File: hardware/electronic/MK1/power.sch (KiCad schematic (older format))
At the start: 3 parts

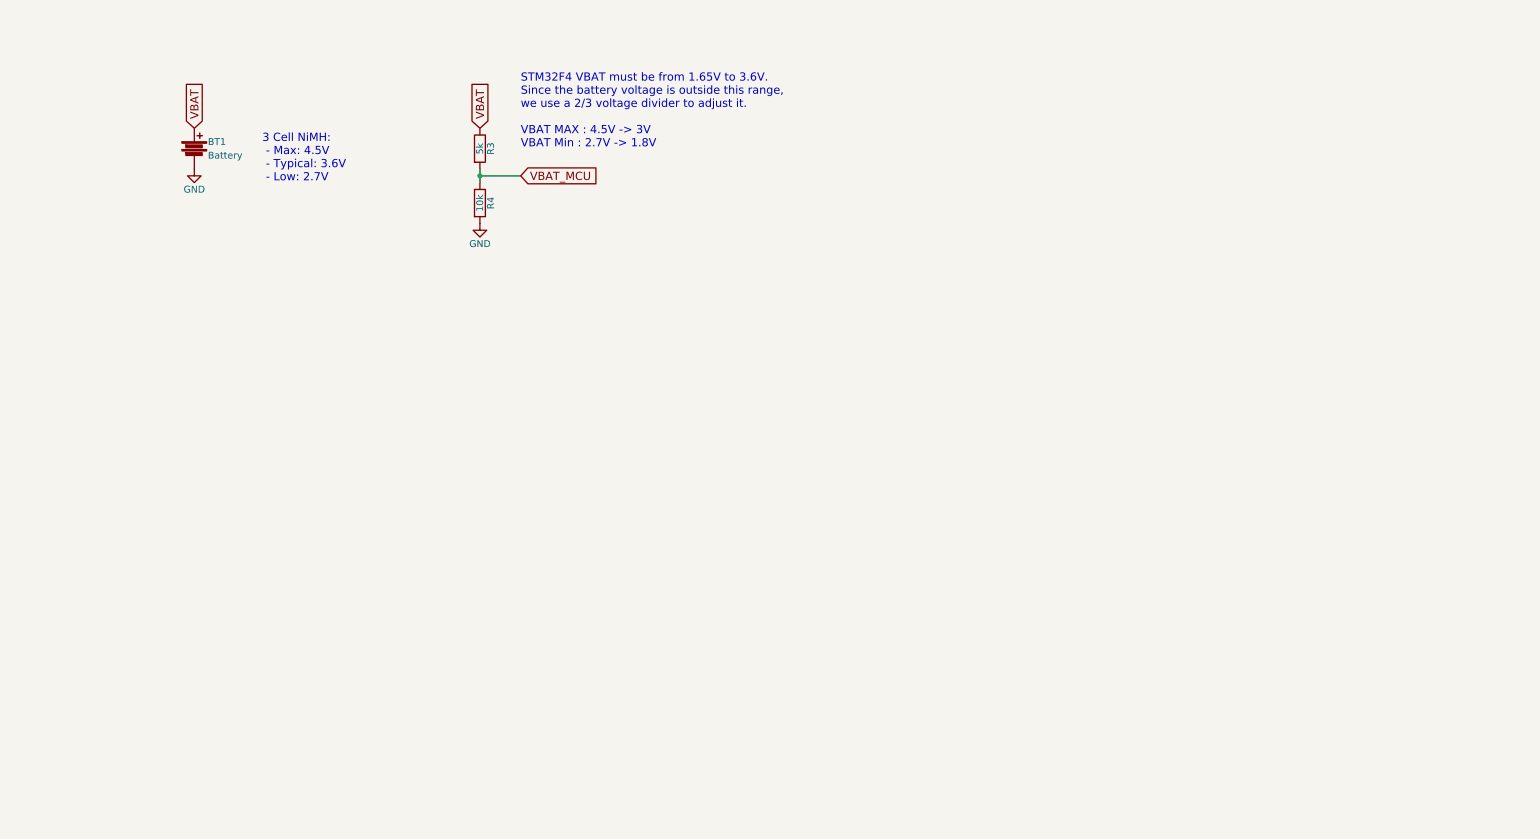
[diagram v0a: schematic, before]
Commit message: HW: Add 3V3 and 5V regulators
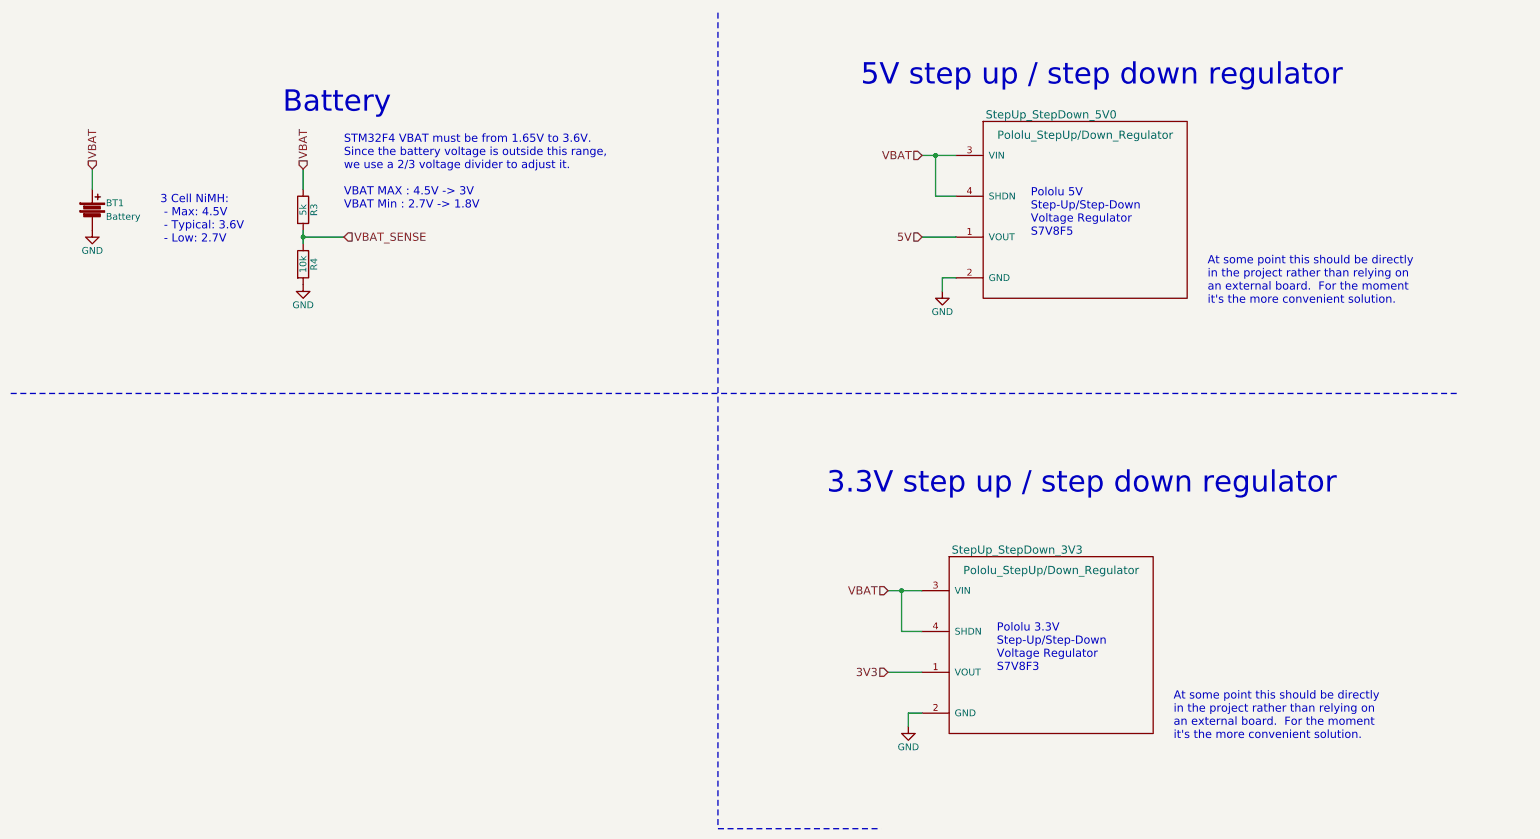
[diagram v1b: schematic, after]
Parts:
- added StepUp_StepDown_3V3, StepUp_StepDown_5V0: Pololu_StepUp/Down_Regulator, symbol Pololu_StepUp/Down_Regulator
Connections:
- net GND: now also StepUp_StepDown_3V3.2 (GND), StepUp_StepDown_5V0.2 (GND)
- net VBAT: now also StepUp_StepDown_3V3.3 (VIN), StepUp_StepDown_3V3.4 (SHDN), StepUp_StepDown_5V0.3 (VIN), StepUp_StepDown_5V0.4 (SHDN)
- net VBAT_MCU renamed VBAT_SENSE
- new net 3V3: StepUp_StepDown_3V3.1 (VOUT)
- new net 5V: StepUp_StepDown_5V0.1 (VOUT)
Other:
- note added: "3.3V step up / step down regulator"
- note added: "5V step up / step down regulator"
- note added: "At some point this should be directly \nin the project rather than relying on \nan external board. For the moment\nit's the more convenient solution."
- note added: "Battery"
- note added: "Pololu 3.3V \nStep-Up/Step-Down\nVoltage Regulator\nS7V8F3"
- note added: "Pololu 5V \nStep-Up/Step-Down\nVoltage Regulator\nS7V8F5"
- moved on the sheet: BT1, R3, R4
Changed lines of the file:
@@
 L Battery BT1
 U 1 1 5885FA38
-P 1900 1550
-F 0 "BT1" H 2000 1600 50  0000 L CNN
-F 1 "Battery" H 2000 1500 50  0000 L CNN
-F 2 "" V 1900 1590 50  0001 C CNN
-F 3 "" V 1900 1590 50  0000 C CNN
-	1    1900 1550
+P 1150 2000
+F 0 "BT1" H 1250 2050 50  0000 L CNN
+F 1 "Battery" H 1250 1950 50  0000 L CNN
+F 2 "" V 1150 2040 50  0001 C CNN
+F 3 "" V 1150 2040 50  0000 C CNN
+	1    1150 2000
 	1    0    0    -1
 $EndComp
@@
 L GND #PWR06
 U 1 1 5885FB0A
-P 1900 1700
-F 0 "#PWR06" H 1900 1450 50  0001 C CNN
-F 1 "GND" H 1900 1550 50  0000 C CNN
-F 2 "" H 1900 1700 50  0000 C CNN
-F 3 "" H 1900 1700 50  0000 C CNN
-	1    1900 1700
+P 1150 2150
+F 0 "#PWR06" H 1150 1900 50  0001 C CNN
+F 1 "GND" H 1150 2000 50  0000 C CNN
+F 2 "" H 1150 2150 50  0000 C CNN
+F 3 "" H 1150 2150 50  0000 C CNN
+	1    1150 2150
 	1    0    0    -1
 $EndComp
-Text GLabel 1900 1400 1    60   Input ~ 0
-VBAT
-Text Notes 2400 1800 0    60   ~ 0
+Text Notes 1650 2250 0    60   ~ 0
 3 Cell NiMH:\n - Max: 4.5V\n - Typical: 3.6V\n - Low: 2.7V
-Text GLabel 4000 1400 1    60   Input ~ 0
-VBAT
 $Comp
 L R R3
 U 1 1 5885FCA2
-P 4000 1550
-F 0 "R3" V 4080 1550 50  0000 C CNN
-F 1 "5k" V 4000 1550 50  0000 C CNN
-F 2 "Resistors_SMD:R_0805" V 3930 1550 50  0001 C CNN
-F 3 "" H 4000 1550 50  0000 C CNN
-	1    4000 1550
+P 2700 2000
+F 0 "R3" V 2780 2000 50  0000 C CNN
+F 1 "5k" V 2700 2000 50  0000 C CNN
+F 2 "Resistors_SMD:R_0805" V 2630 2000 50  0001 C CNN
+F 3 "" H 2700 2000 50  0000 C CNN
+	1    2700 2000
 	1    0    0    -1
 $EndComp
@@
 L R R4
 U 1 1 5885FCD9
-P 4000 1950
-F 0 "R4" V 4080 1950 50  0000 C CNN
-F 1 "10k" V 4000 1950 50  0000 C CNN
-F 2 "Resistors_SMD:R_0805" V 3930 1950 50  0001 C CNN
-F 3 "" H 4000 1950 50  0000 C CNN
-	1    4000 1950
+P 2700 2400
+F 0 "R4" V 2780 2400 50  0000 C CNN
+F 1 "10k" V 2700 2400 50  0000 C CNN
+F 2 "Resistors_SMD:R_0805" V 2630 2400 50  0001 C CNN
+F 3 "" H 2700 2400 50  0000 C CNN
+	1    2700 2400
 	1    0    0    -1
 $EndComp
 Wire Wire Line
-	4000 1700 4000 1800
+	2700 2150 2700 2250
 Wire Wire Line
-	4000 1750 4300 1750
-Connection ~ 4000 1750
+	2700 2200 3000 2200
+Connection ~ 2700 2200
 $Comp
 L GND #PWR07
 U 1 1 5885FD97
-P 4000 2100
-F 0 "#PWR07" H 4000 1850 50  0001 C CNN
-F 1 "GND" H 4000 1950 50  0000 C CNN
-F 2 "" H 4000 2100 50  0000 C CNN
-F 3 "" H 4000 2100 50  0000 C CNN
-	1    4000 2100
+P 2700 2550
+F 0 "#PWR07" H 2700 2300 50  0001 C CNN
+F 1 "GND" H 2700 2400 50  0000 C CNN
+F 2 "" H 2700 2550 50  0000 C CNN
+F 3 "" H 2700 2550 50  0000 C CNN
+	1    2700 2550
 	1    0    0    -1
 $EndComp
-Text GLabel 4300 1750 2    60   Input ~ 0
-VBAT_MCU
-Text Notes 4300 1550 0    60   ~ 0
+Text Notes 3000 2000 0    60   ~ 0
 STM32F4 VBAT must be from 1.65V to 3.6V.\nSince the battery voltage is outside this range,\nwe use a 2/3 voltage divider to adjust it.\n\nVBAT MAX : 4.5V -> 3V\nVBAT Min : 2.7V -> 1.8V
+Text HLabel 3000 2200 2    60   Input ~ 0
+VBAT_SENSE
+Wire Wire Line
+	1150 1850 1150 1700
+Wire Wire Line
+	2700 1850 2700 1700
+Text HLabel 1150 1700 1    60   Input ~ 0
+VBAT
+Text HLabel 2700 1700 1    60   Input ~ 0
+VBAT
+Text Notes 2550 1300 0    157  ~ 0
+Battery
+Text Notes 8050 2200 0    60   ~ 0
+Pololu 5V \nStep-Up/Step-Down\nVoltage Regulator\nS7V8F5
+Connection ~ 7350 1600
+Wire Wire Line
+	7350 1900 7350 1600
+Wire Wire Line
+	7500 1900 7350 1900
+Wire Wire Line
+	7500 2200 7250 2200
+Wire Wire Line
+	7400 2500 7400 2600
+Wire Wire Line
+	7500 2500 7400 2500
+Wire Wire Line
+	7500 1600 7250 1600
+$Comp
+L Pololu_StepUp/Down_Regulator StepUp_StepDown_5V0
+U 1 1 588A675B
+P 7700 1350
+F 0 "StepUp_StepDown_5V0" H 8200 1400 60  0000 C CNN
+F 1 "Pololu_StepUp/Down_Regulator" H 8450 1250 60  0000 C CNN
+F 2 "" H 7700 1350 60  0001 C CNN
+F 3 "" H 7700 1350 60  0001 C CNN
+	1    7700 1350
+	1    0    0    -1
+$EndComp
+Text Notes 9350 2700 0    60   ~ 0
+At some point this should be directly \nin the project rather than relying on \nan external board.  For the moment\nit's the more convenient solution.
+Text Notes 6800 1100 0    157  ~ 0
+5V step up / step down regulator
+Text HLabel 7250 1600 0    60   Input ~ 0
+VBAT
+Text HLabel 7250 2200 0    60   Input ~ 0
+5V
+$Comp
+L GND #PWR08
+U 1 1 588A1F16
+P 7400 2600
+F 0 "#PWR08" H 7400 2350 50  0001 C CNN
+F 1 "GND" H 7400 2450 50  0000 C CNN
+F 2 "" H 7400 2600 50  0000 C CNN
+F 3 "" H 7400 2600 50  0000 C CNN
+	1    7400 2600
+	1    0    0    -1
+$EndComp
+Text Notes 7800 5400 0    60   ~ 0
+Pololu 3.3V \nStep-Up/Step-Down\nVoltage Regulator\nS7V8F3
+Connection ~ 7100 4800
+Wire Wire Line
+	7100 5100 7100 4800
+Wire Wire Line
+	7250 5100 7100 5100
+Wire Wire Line
+	7250 5400 7000 5400
+Wire Wire Line
+	7150 5700 7150 5800
+Wire Wire Line
+	7250 5700 7150 5700
+Wire Wire Line
+	7250 4800 7000 4800
+$Comp
+L Pololu_StepUp/Down_Regulator StepUp_StepDown_3V3
+U 1 1 588A6FCC
+P 7450 4550
+F 0 "StepUp_StepDown_3V3" H 7950 4600 60  0000 C CNN
+F 1 "Pololu_StepUp/Down_Regulator" H 8200 4450 60  0000 C CNN
+F 2 "" H 7450 4550 60  0001 C CNN
+F 3 "" H 7450 4550 60  0001 C CNN
+	1    7450 4550
+	1    0    0    -1
+$EndComp
+Text Notes 9100 5900 0    60   ~ 0
+At some point this should be directly \nin the project rather than relying on \nan external board.  For the moment\nit's the more convenient solution.
+Text Notes 6550 4100 0    157  ~ 0
+3.3V step up / step down regulator
+Text HLabel 7000 4800 0    60   Input ~ 0
+VBAT
+Text HLabel 7000 5400 0    60   Input ~ 0
+3V3
+$Comp
+L GND #PWR?
+U 1 1 588A6FD6
+P 7150 5800
+F 0 "#PWR?" H 7150 5550 50  0001 C CNN
+F 1 "GND" H 7150 5650 50  0000 C CNN
+F 2 "" H 7150 5800 50  0000 C CNN
+F 3 "" H 7150 5800 50  0000 C CNN
+	1    7150 5800
+	1    0    0    -1
+$EndComp
+Wire Notes Line
+	550  3350 11200 3350
+Wire Notes Line
+	5750 550  5750 6550
+Wire Notes Line
+	5750 6550 6950 6550
 $EndSCHEMATC

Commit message: HW: Add an AdaFruit BNO055 breakout backup for the IMU
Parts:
- StepUp_StepDown_3V3, StepUp_StepDown_5V0: footprint (none) -> OPAVES_Footprints:Pololu_StepUp_StepDown_Regulator
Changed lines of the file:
@@
 F 0 "StepUp_StepDown_5V0" H 8200 1400 60  0000 C CNN
 F 1 "Pololu_StepUp/Down_Regulator" H 8450 1250 60  0000 C CNN
-F 2 "" H 7700 1350 60  0001 C CNN
+F 2 "OPAVES_Footprints:Pololu_StepUp_StepDown_Regulator" H 7700 1350 60  0001 C CNN
 F 3 "" H 7700 1350 60  0001 C CNN
 	1    7700 1350
@@
 F 0 "StepUp_StepDown_3V3" H 7950 4600 60  0000 C CNN
 F 1 "Pololu_StepUp/Down_Regulator" H 8200 4450 60  0000 C CNN
-F 2 "" H 7450 4550 60  0001 C CNN
+F 2 "OPAVES_Footprints:Pololu_StepUp_StepDown_Regulator" H 7450 4550 60  0001 C CNN
 F 3 "" H 7450 4550 60  0001 C CNN
 	1    7450 4550
@@
 3V3
 $Comp
-L GND #PWR?
+L GND #PWR09
 U 1 1 588A6FD6
 P 7150 5800
-F 0 "#PWR?" H 7150 5550 50  0001 C CNN
+F 0 "#PWR09" H 7150 5550 50  0001 C CNN
 F 1 "GND" H 7150 5650 50  0000 C CNN
 F 2 "" H 7150 5800 50  0000 C CNN

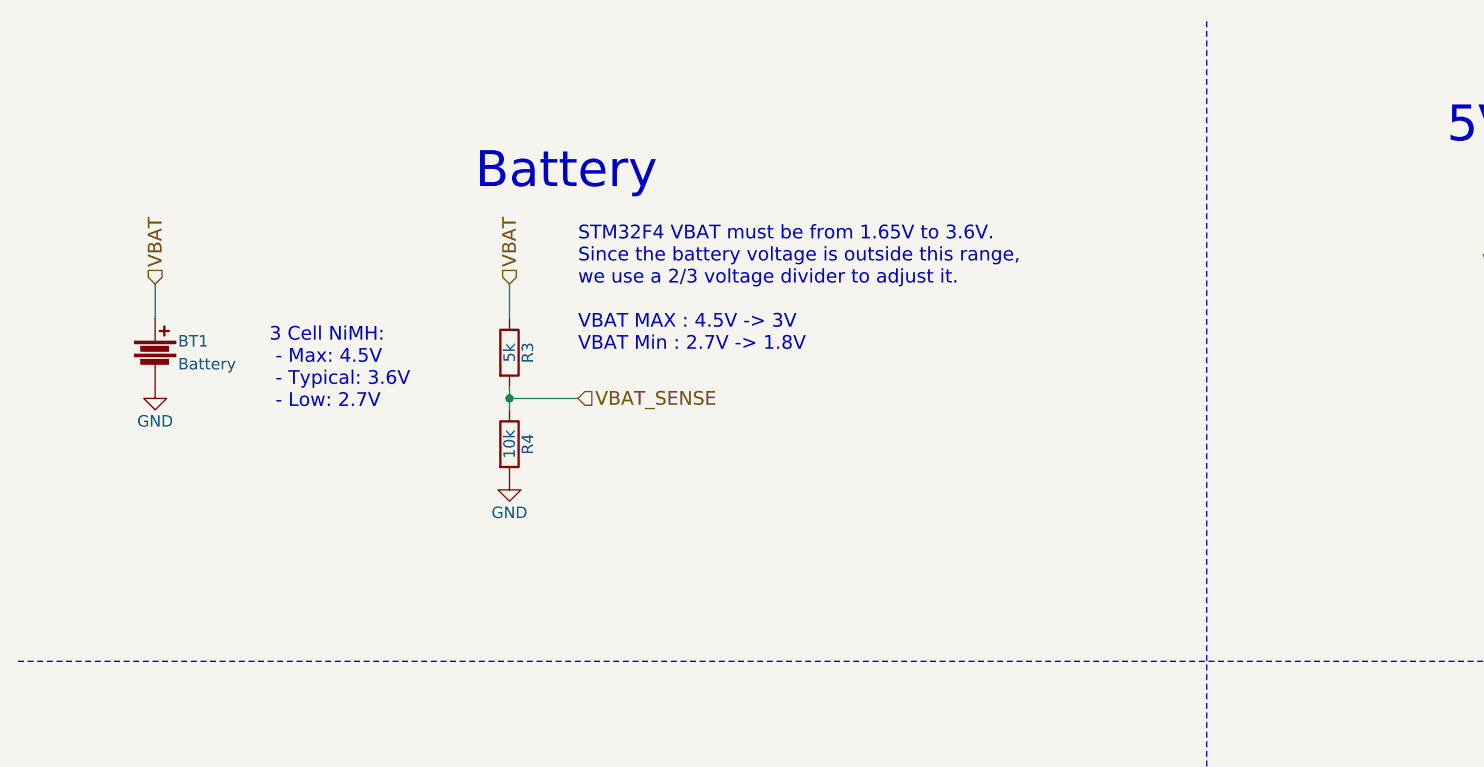
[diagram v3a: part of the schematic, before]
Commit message: HW: Add battery connector
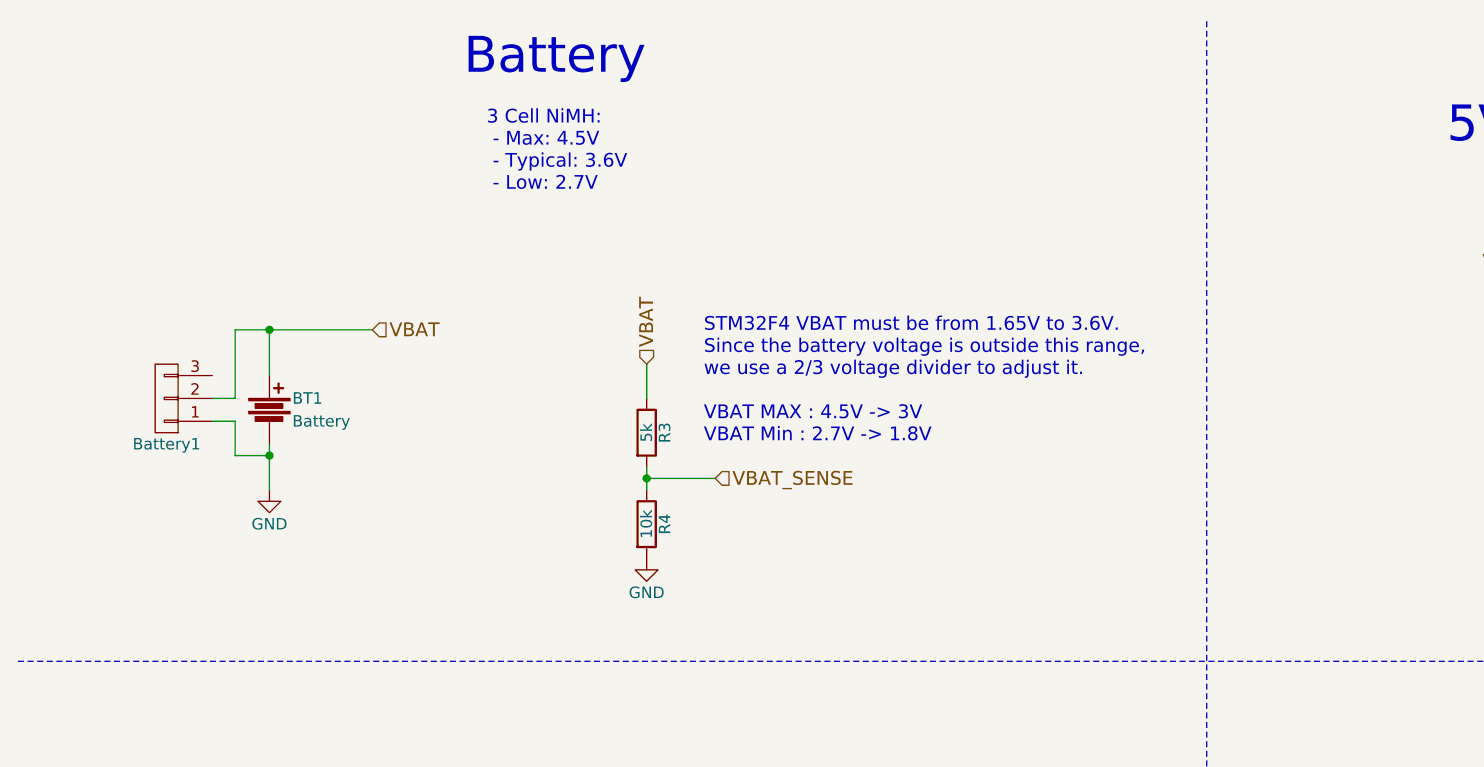
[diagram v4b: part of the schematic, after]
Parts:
- added Battery1: CONN_01X03, Pin_Headers:Pin_Header_Angled_1x03, symbol CONN_01X03
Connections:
- net GND: now also Battery1.1 (P1)
- net VBAT: now also Battery1.2 (P2)
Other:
- moved on the sheet: BT1, R3, R4
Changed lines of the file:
@@
 L Battery BT1
 U 1 1 5885FA38
-P 1150 2000
-F 0 "BT1" H 1250 2050 50  0000 L CNN
-F 1 "Battery" H 1250 1950 50  0000 L CNN
-F 2 "" V 1150 2040 50  0001 C CNN
-F 3 "" V 1150 2040 50  0000 C CNN
-	1    1150 2000
+P 1650 2250
+F 0 "BT1" H 1750 2300 50  0000 L CNN
+F 1 "Battery" H 1750 2200 50  0000 L CNN
+F 2 "" V 1650 2290 50  0001 C CNN
+F 3 "" V 1650 2290 50  0000 C CNN
+	1    1650 2250
 	1    0    0    -1
 $EndComp
@@
 L GND #PWR09
 U 1 1 5885FB0A
-P 1150 2150
-F 0 "#PWR09" H 1150 1900 50  0001 C CNN
-F 1 "GND" H 1150 2000 50  0000 C CNN
-F 2 "" H 1150 2150 50  0000 C CNN
-F 3 "" H 1150 2150 50  0000 C CNN
-	1    1150 2150
+P 1650 2600
+F 0 "#PWR09" H 1650 2350 50  0001 C CNN
+F 1 "GND" H 1650 2450 50  0000 C CNN
+F 2 "" H 1650 2600 50  0000 C CNN
+F 3 "" H 1650 2600 50  0000 C CNN
+	1    1650 2600
 	1    0    0    -1
 $EndComp
-Text Notes 1650 2250 0    60   ~ 0
+Text Notes 2600 1300 0    60   ~ 0
 3 Cell NiMH:\n - Max: 4.5V\n - Typical: 3.6V\n - Low: 2.7V
 $Comp
 L R R3
 U 1 1 5885FCA2
-P 2700 2000
-F 0 "R3" V 2780 2000 50  0000 C CNN
-F 1 "5k" V 2700 2000 50  0000 C CNN
-F 2 "Resistors_SMD:R_0805" V 2630 2000 50  0001 C CNN
-F 3 "" H 2700 2000 50  0000 C CNN
-	1    2700 2000
+P 3300 2350
+F 0 "R3" V 3380 2350 50  0000 C CNN
+F 1 "5k" V 3300 2350 50  0000 C CNN
+F 2 "Resistors_SMD:R_0805" V 3230 2350 50  0001 C CNN
+F 3 "" H 3300 2350 50  0000 C CNN
+	1    3300 2350
 	1    0    0    -1
 $EndComp
@@
 L R R4
 U 1 1 5885FCD9
-P 2700 2400
-F 0 "R4" V 2780 2400 50  0000 C CNN
-F 1 "10k" V 2700 2400 50  0000 C CNN
-F 2 "Resistors_SMD:R_0805" V 2630 2400 50  0001 C CNN
-F 3 "" H 2700 2400 50  0000 C CNN
-	1    2700 2400
+P 3300 2750
+F 0 "R4" V 3380 2750 50  0000 C CNN
+F 1 "10k" V 3300 2750 50  0000 C CNN
+F 2 "Resistors_SMD:R_0805" V 3230 2750 50  0001 C CNN
+F 3 "" H 3300 2750 50  0000 C CNN
+	1    3300 2750
 	1    0    0    -1
 $EndComp
 Wire Wire Line
-	2700 2150 2700 2250
+	3300 2500 3300 2600
 Wire Wire Line
-	2700 2200 3000 2200
-Connection ~ 2700 2200
+	3300 2550 3600 2550
+Connection ~ 3300 2550
 $Comp
 L GND #PWR010
 U 1 1 5885FD97
-P 2700 2550
-F 0 "#PWR010" H 2700 2300 50  0001 C CNN
-F 1 "GND" H 2700 2400 50  0000 C CNN
-F 2 "" H 2700 2550 50  0000 C CNN
-F 3 "" H 2700 2550 50  0000 C CNN
-	1    2700 2550
+P 3300 2900
+F 0 "#PWR010" H 3300 2650 50  0001 C CNN
+F 1 "GND" H 3300 2750 50  0000 C CNN
+F 2 "" H 3300 2900 50  0000 C CNN
+F 3 "" H 3300 2900 50  0000 C CNN
+	1    3300 2900
 	1    0    0    -1
 $EndComp
-Text Notes 3000 2000 0    60   ~ 0
+Text Notes 3550 2400 0    60   ~ 0
 STM32F4 VBAT must be from 1.65V to 3.6V.\nSince the battery voltage is outside this range,\nwe use a 2/3 voltage divider to adjust it.\n\nVBAT MAX : 4.5V -> 3V\nVBAT Min : 2.7V -> 1.8V
-Text HLabel 3000 2200 2    60   Input ~ 0
+Text HLabel 3600 2550 2    60   Input ~ 0
 VBAT_SENSE
 Wire Wire Line
-	1150 1850 1150 1700
-Wire Wire Line
-	2700 1850 2700 1700
-Text HLabel 1150 1700 1    60   Input ~ 0
+	3300 2200 3300 2050
+Text HLabel 2100 1900 2    60   Input ~ 0
 VBAT
-Text HLabel 2700 1700 1    60   Input ~ 0
+Text HLabel 3300 2050 1    60   Input ~ 0
 VBAT
-Text Notes 2550 1300 0    157  ~ 0
+Text Notes 2500 800  0    157  ~ 0
 Battery
 Text Notes 8050 2200 0    60   ~ 0
@@
 Wire Notes Line
 	5750 6550 6950 6550
+Wire Wire Line
+	1650 2400 1650 2600
+Wire Wire Line
+	1500 1900 2100 1900
+$Comp
+L CONN_01X03 Battery1
+U 1 1 588B953B
+P 1200 2200
+F 0 "Battery1" H 1200 2400 50  0000 C CNN
+F 1 "CONN_01X03" V 1300 2200 50  0001 C CNN
+F 2 "Pin_Headers:Pin_Header_Angled_1x03" H 1200 2200 50  0001 C CNN
+F 3 "" H 1200 2200 50  0000 C CNN
+	1    1200 2200
+	-1   0    0    1
+$EndComp
+Wire Wire Line
+	1500 2200 1400 2200
+Wire Wire Line
+	1500 1900 1500 2200
+Wire Wire Line
+	1650 2100 1650 1900
+Connection ~ 1650 1900
+Wire Wire Line
+	1400 2300 1500 2300
+Wire Wire Line
+	1500 2300 1500 2450
+Wire Wire Line
+	1500 2450 1650 2450
+Connection ~ 1650 2450
 $EndSCHEMATC

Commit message: HW: Add steering servo connector
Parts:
- Battery1: footprint Pin_Headers:Pin_Header_Angled_1x03 -> Pin_Headers:Pin_Header_Straight_1x03
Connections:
- no-connect marks 0 -> 1
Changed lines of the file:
@@
 F 0 "Battery1" H 1200 2400 50  0000 C CNN
 F 1 "CONN_01X03" V 1300 2200 50  0001 C CNN
-F 2 "Pin_Headers:Pin_Header_Angled_1x03" H 1200 2200 50  0001 C CNN
+F 2 "Pin_Headers:Pin_Header_Straight_1x03" H 1200 2200 50  0001 C CNN
 F 3 "" H 1200 2200 50  0000 C CNN
 	1    1200 2200
@@
 	1500 2450 1650 2450
 Connection ~ 1650 2450
+NoConn ~ 1400 2100
 $EndSCHEMATC
